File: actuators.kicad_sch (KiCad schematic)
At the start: 12 parts, among them J3 ServoCH1, J4 ServoCH2, J5 GPIO Breakout

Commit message: review changes
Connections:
- net GND: now also J5.10 (Pin_10)
- no-connect marks 1 -> 0
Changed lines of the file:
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@@
 		(color 0 0 0 0)
-	)
-	(no_connect
-		(at 227.838 86.36)
 	)
 	(wire
@@
 					(unit 1)
 				)
+			)
+		)
+	)
+	(symbol
+		(lib_id "power:GND")
+		(at 227.838 86.36 270)
+		(unit 1)
+		(exclude_from_sim no)
+		(in_bom yes)
+		(on_board yes)
+		(dnp no)
+		(fields_autoplaced yes)
+		(property "Reference" "#PWR085"
+			(at 221.488 86.36 0)
+			(effects
+				(font
+					(size 1.27 1.27)
+				)
+				(hide yes)
+			)
+		)
+		(property "Value" "GND"
+			(at 224.6631 86.7938 90)
+			(effects
+				(font
+					(size 1.27 1.27)
+				)
+				(justify right)
+			)
+		)
+		(property "Footprint" ""
+			(at 227.838 86.36 0)
+			(effects
+				(font
+					(size 1.27 1.27)
+				)
+				(hide yes)
+			)
+		)
+		(property "Datasheet" ""
+			(at 227.838 86.36 0)
+			(effects
+				(font
+					(size 1.27 1.27)
+				)
+				(hide yes)
+			)
+		)
+		(property "Description" ""
+			(at 227.838 86.36 0)
+			(effects
+				(font
+					(size 1.27 1.27)
+				)
+				(hide yes)
+			)
+		)
+		(pin "1"
+		)
+		(instances
+			(project "Ricardo-Stark"
+				(path "/7db990e4-92e1-4f99-b4d2-435bbec1ba83/5f0880ee-ff3b-4d6c-b43c-55333f7e65e0"
+					(reference "#PWR085")
+					(unit 1)
+				)

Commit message: commit
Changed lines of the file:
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@@
-		)
-	)
-	(label "Servo2PWM"
-		(at 143.51 83.82 180)
-		(fields_autoplaced yes)
-		(effects
-			(font
-				(size 1.27 1.27)
-			)
-			(justify right bottom)
-		)
-	)
-	(label "Servo1PWM"
-		(at 142.24 68.58 180)
-		(fields_autoplaced yes)
-		(effects
-			(font
-				(size 1.27 1.27)
-			)
-			(justify right bottom)
-		)
-	)
-	(label "ServoV_LOG"
-		(at 137.16 106.68 180)
-		(fields_autoplaced yes)
-		(effects
-			(font
-				(size 1.27 1.27)
-			)
-			(justify right bottom)
 		)
 	)
@@
 	(hierarchical_label "SERVO1"
 		(shape bidirectional)
-		(at 153.67 68.58 180)
+		(at 142.24 68.58 180)
 		(fields_autoplaced yes)
 		(effects
@@
 	(hierarchical_label "SERVO_LOG"
 		(shape output)
-		(at 151.13 106.68 180)
+		(at 137.16 106.68 180)
 		(fields_autoplaced yes)
 		(effects
@@
 	(hierarchical_label "SERVO2"
 		(shape bidirectional)
-		(at 153.67 83.82 180)
+		(at 143.51 83.82 180)
 		(fields_autoplaced yes)
 		(effects

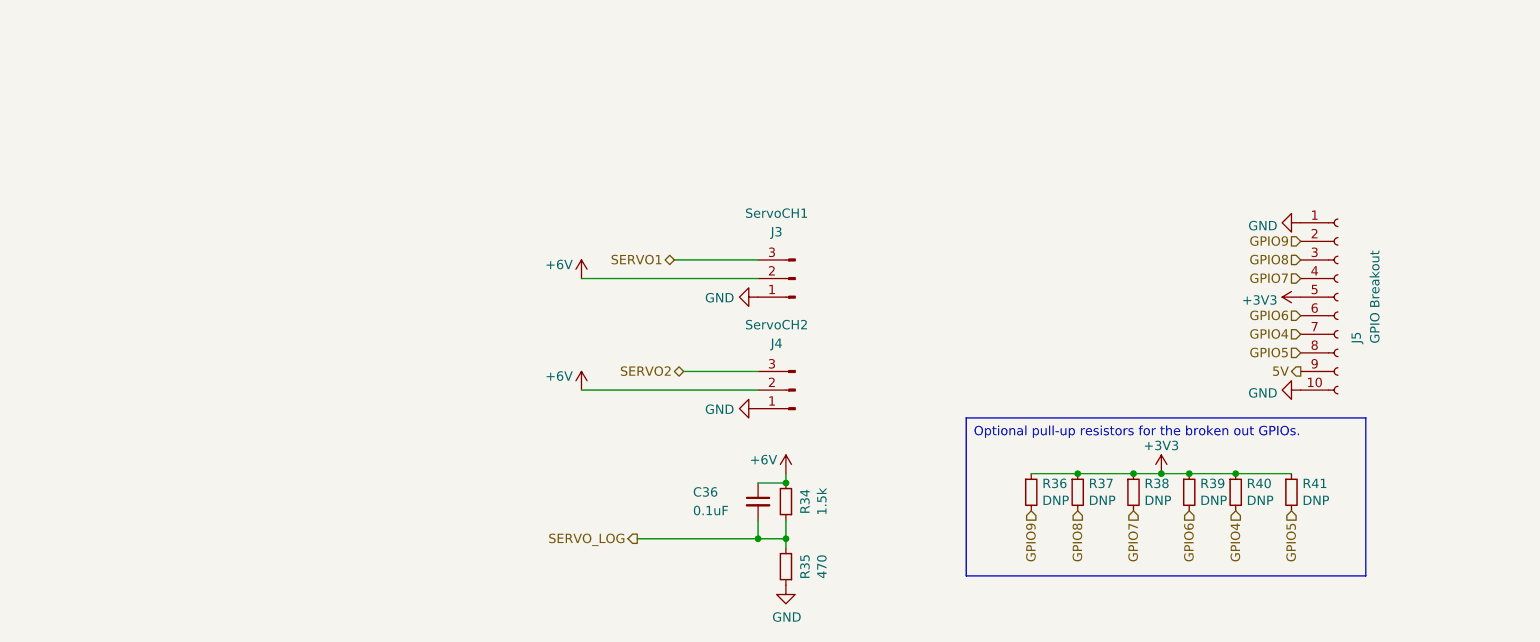
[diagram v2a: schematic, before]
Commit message: reshuffled layout
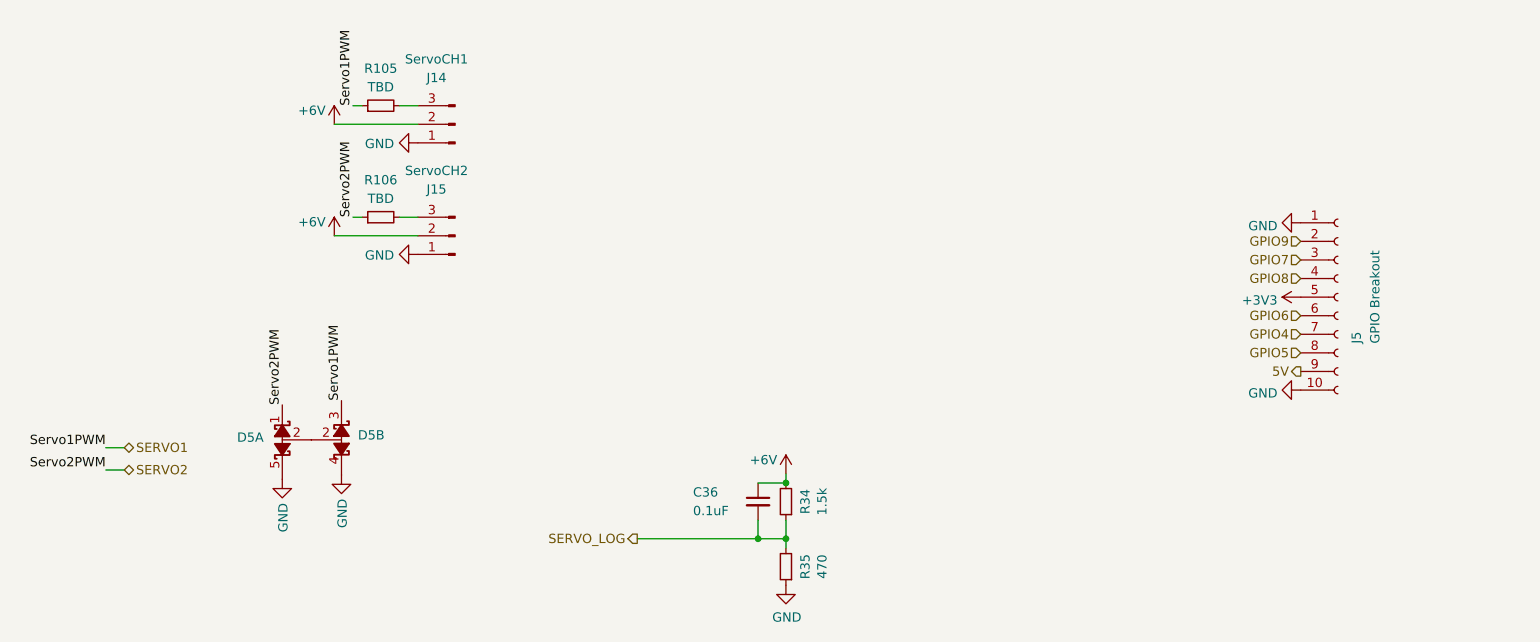
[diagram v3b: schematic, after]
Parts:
- removed J3: ServoCH1, Connector_Molex:Molex_Nano-Fit_105313-xx03_1x03_P2.50mm_Horizontal, symbol Connector:Conn_01x03_Male
- removed J4: ServoCH2, Connector_Molex:Molex_Nano-Fit_105313-xx03_1x03_P2.50mm_Horizontal, symbol Connector:Conn_01x03_Male
- removed R36, R37, R38, R39, R40, R41: DNP, Resistor_SMD:R_0402_1005Metric, symbol Device:R_Small
- added D5: ~, Package_TO_SOT_SMD:SOT-353_SC-70-5, symbol iclr:CPDV5-3V3UP
- added J14: ServoCH1, Connector_Molex:Molex_Nano-Fit_105313-xx03_1x03_P2.50mm_Horizontal, symbol Connector:Conn_01x03_Male
- added J15: ServoCH2, Connector_Molex:Molex_Nano-Fit_105313-xx03_1x03_P2.50mm_Horizontal, symbol Connector:Conn_01x03_Male
- added R105, R106: TBD, Resistor_SMD:R_0402_1005Metric, symbol Device:R_Small
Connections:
- net +6V: now also J14.2 (Pin_2), J15.2 (Pin_2)
- net GND: now also D5.4, D5.5, J14.1 (Pin_1), J15.1 (Pin_1)
- net GPIO7: now also J5.3 (Pin_3); no longer J5.4 (Pin_4)
- net GPIO8: now also J5.4 (Pin_4); no longer J5.3 (Pin_3)
- net SERVO1: now also D5.3, R105.1
- net SERVO2: now also D5.1, R106.1
- new net: J14.3 (Pin_3), R105.2
- new net: D5.2, D5.2
- new net: J15.3 (Pin_3), R106.2

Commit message: more changes
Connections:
- net +3V3: now also J5.4 (Pin_4); no longer J5.5 (Pin_5)
- net 5V: now also J5.3 (Pin_3); no longer J5.9 (Pin_9)
- net GND: now also J5.2 (Pin_2); no longer J5.10 (Pin_10)
- net GPIO4: now also J5.9 (Pin_9); no longer J5.7 (Pin_7)
- net GPIO5: now also J5.6 (Pin_6); no longer J5.8 (Pin_8)
- net GPIO6: now also J5.8 (Pin_8); no longer J5.6 (Pin_6)
- net GPIO7: now also J5.10 (Pin_10); no longer J5.3 (Pin_3)
- net GPIO8: now also J5.5 (Pin_5); no longer J5.4 (Pin_4)
- net GPIO9: now also J5.7 (Pin_7); no longer J5.2 (Pin_2)

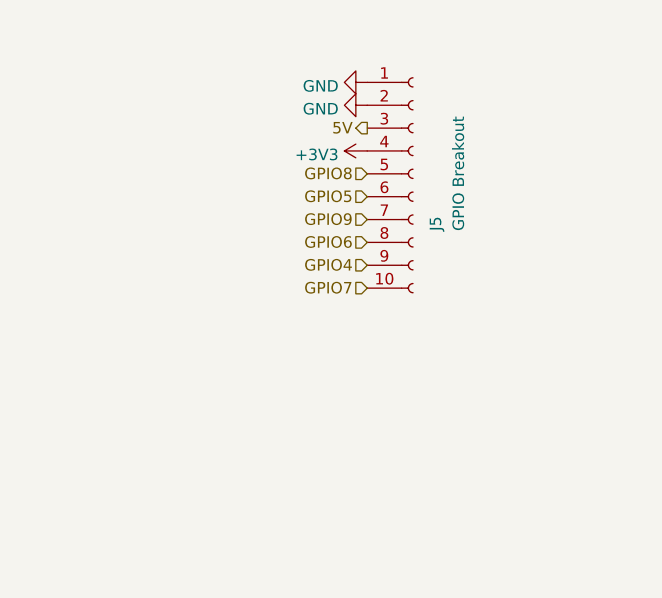
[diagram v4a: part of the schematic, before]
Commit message: Changed sd card holder
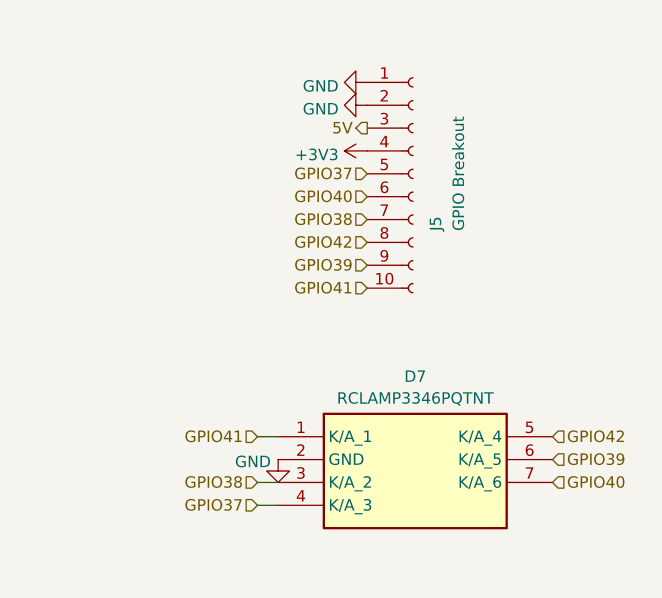
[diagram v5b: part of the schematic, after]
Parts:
- added D7: RCLAMP3346PQTNT, iclr:RCLAMP3346PQTNT, symbol iclr:RCLAMP3346PQTNT
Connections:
- net GND: now also D7.2 (GND)
- net GPIO4 renamed GPIO39
- net GPIO39: now also D7.6 (K/A_5)
- net GPIO5 renamed GPIO40
- net GPIO40: now also D7.7 (K/A_6)
- net GPIO6 renamed GPIO42
- net GPIO42: now also D7.5 (K/A_4)
- net GPIO7 renamed GPIO41
- net GPIO41: now also D7.1 (K/A_1)
- net GPIO8 renamed GPIO37
- net GPIO37: now also D7.4 (K/A_3)
- net GPIO9 renamed GPIO38
- net GPIO38: now also D7.3 (K/A_2)
